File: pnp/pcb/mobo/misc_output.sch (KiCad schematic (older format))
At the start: 45 parts, among them J10 MF3, J11 MF4, J12 DOWNWARDS_LIGHT, J13 UPWARDS_LIGHT, J14 5V_INJECTION, J16 RS-485_2, J17 RS-485_3, J21 AUX1, J22 AUX2, J23 QWIIC1, J24 QWIIC2, J25 RS-485_1, J6 SERVO1, J7 SERVO2, J8 MF1, J9 MF2, Q1 IRF540N, Q2 IRF540N, Q3 IRF540N, Q4 IRF540N, U15 TC4424A, U16 TC4424A, U2 SP3485EN, U3 SP3485EN, U4 SP3485EN

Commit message: Add 24VDC support
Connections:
- net labels added: VDC
- net labels removed: +12V
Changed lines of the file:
@@
 	3325 3050 3325 2850
-$Comp
-L power:+12V #PWR0133
-U 1 1 5EBF89E8
-P 3325 2150
-F 0 "#PWR0133" H 3325 2000 50  0001 C CNN
-F 1 "+12V" H 3340 2323 50  0000 C CNN
-F 2 "" H 3325 2150 50  0001 C CNN
-F 3 "" H 3325 2150 50  0001 C CNN
-	1    3325 2150
-	1    0    0    -1
-$EndComp
 $Comp
 L Device:R_Small R2
@@
 $EndComp
 $Comp
-L power:+12V #PWR0136
-U 1 1 5EC0DF79
-P 3325 3550
-F 0 "#PWR0136" H 3325 3400 50  0001 C CNN
-F 1 "+12V" H 3340 3723 50  0000 C CNN
-F 2 "" H 3325 3550 50  0001 C CNN
-F 3 "" H 3325 3550 50  0001 C CNN
-	1    3325 3550
-	1    0    0    -1
-$EndComp
-$Comp
 L Device:R_Small R3
 U 1 1 5EC0DF80
@@
 $EndComp
 $Comp
-L power:+12V #PWR0139
-U 1 1 5EC1398B
-P 3325 4950
-F 0 "#PWR0139" H 3325 4800 50  0001 C CNN
-F 1 "+12V" H 3340 5123 50  0000 C CNN
-F 2 "" H 3325 4950 50  0001 C CNN
-F 3 "" H 3325 4950 50  0001 C CNN
-	1    3325 4950
-	1    0    0    -1
-$EndComp
-$Comp
 L Device:R_Small R4
 U 1 1 5EC13992
@@
 	1    3125 6550
 	-1   0    0    1
-$EndComp
-$Comp
-L power:+12V #PWR0142
-U 1 1 5EC17A7D
-P 3325 6350
-F 0 "#PWR0142" H 3325 6200 50  0001 C CNN
-F 1 "+12V" H 3340 6523 50  0000 C CNN
-F 2 "" H 3325 6350 50  0001 C CNN
-F 3 "" H 3325 6350 50  0001 C CNN
-	1    3325 6350
-	1    0    0    -1
 $EndComp
 $Comp
@@
 Wire Wire Line
 	3475 2150 3325 2150
-Connection ~ 3325 2150
 Wire Wire Line
 	3325 2250 3325 2150
@@
 Wire Wire Line
 	3475 3550 3325 3550
-Connection ~ 3325 3550
 Wire Wire Line
 	3475 3850 3325 3850
@@
 Wire Wire Line
 	3475 4950 3325 4950
-Connection ~ 3325 4950
 Wire Wire Line
 	3475 5250 3325 5250
@@
 Wire Wire Line
 	3475 6350 3325 6350
-Connection ~ 3325 6350
 $Comp
 L index:TC4424A U15
@@
 $EndComp
 $Comp
-L power:+12V #PWR01
-U 1 1 600410AF
-P 1700 3075
-F 0 "#PWR01" H 1700 2925 50  0001 C CNN
-F 1 "+12V" H 1715 3248 50  0000 C CNN
-F 2 "" H 1700 3075 50  0001 C CNN
-F 3 "" H 1700 3075 50  0001 C CNN
-	1    1700 3075
-	1    0    0    -1
-$EndComp
-$Comp
 L index:TC4424A U16
 U 1 1 6005F5C2
@@
 	1    0    0    -1
 $EndComp
-$Comp
-L power:+12V #PWR03
-U 1 1 6005F5D0
+Wire Wire Line
+	2225 5450 2225 6050
+Wire Wire Line
+	2225 6150 2225 6850
+Wire Wire Line
+	2875 4450 3325 4450
+Connection ~ 3325 4450
+Wire Wire Line
+	2875 3050 3325 3050
+Connection ~ 3325 3050
+Wire Wire Line
+	2875 5850 3325 5850
+Connection ~ 3325 5850
+Wire Wire Line
+	2875 7250 3325 7250
+Connection ~ 3325 7250
+$Comp
+L power:VDC #PWR011
+U 1 1 5FE2C7FC
+P 3325 2150
+F 0 "#PWR011" H 3325 2050 50  0001 C CNN
+F 1 "VDC" H 3340 2323 50  0000 C CNN
+F 2 "" H 3325 2150 50  0001 C CNN
+F 3 "" H 3325 2150 50  0001 C CNN
+	1    3325 2150
+	1    0    0    -1
+$EndComp
+Connection ~ 3325 2150
+$Comp
+L power:VDC #PWR012
+U 1 1 5FE2D669
+P 3325 3550
+F 0 "#PWR012" H 3325 3450 50  0001 C CNN
+F 1 "VDC" H 3340 3723 50  0000 C CNN
+F 2 "" H 3325 3550 50  0001 C CNN
+F 3 "" H 3325 3550 50  0001 C CNN
+	1    3325 3550
+	1    0    0    -1
+$EndComp
+Connection ~ 3325 3550
+$Comp
+L power:VDC #PWR013
+U 1 1 5FE329DB
+P 3325 4950
+F 0 "#PWR013" H 3325 4850 50  0001 C CNN
+F 1 "VDC" H 3340 5123 50  0000 C CNN
+F 2 "" H 3325 4950 50  0001 C CNN
+F 3 "" H 3325 4950 50  0001 C CNN
+	1    3325 4950
+	1    0    0    -1
+$EndComp
+Connection ~ 3325 4950
+$Comp
+L power:VDC #PWR014
+U 1 1 5FE341D0
+P 3325 6350
+F 0 "#PWR014" H 3325 6250 50  0001 C CNN
+F 1 "VDC" H 3340 6523 50  0000 C CNN
+F 2 "" H 3325 6350 50  0001 C CNN
+F 3 "" H 3325 6350 50  0001 C CNN
+	1    3325 6350
+	1    0    0    -1
+$EndComp
+Connection ~ 3325 6350
+$Comp
+L power:+5V #PWR010
+U 1 1 5FE3A03F
 P 1700 5850
-F 0 "#PWR03" H 1700 5700 50  0001 C CNN
-F 1 "+12V" H 1715 6023 50  0000 C CNN
+F 0 "#PWR010" H 1700 5700 50  0001 C CNN
+F 1 "+5V" H 1715 6023 50  0000 C CNN
 F 2 "" H 1700 5850 50  0001 C CNN
 F 3 "" H 1700 5850 50  0001 C CNN
@@
 	1    0    0    -1
 $EndComp
-Wire Wire Line
-	2225 5450 2225 6050
-Wire Wire Line
-	2225 6150 2225 6850
-Wire Wire Line
-	2875 4450 3325 4450
-Connection ~ 3325 4450
-Wire Wire Line
-	2875 3050 3325 3050
-Connection ~ 3325 3050
-Wire Wire Line
-	2875 5850 3325 5850
-Connection ~ 3325 5850
-Wire Wire Line
-	2875 7250 3325 7250
-Connection ~ 3325 7250
+$Comp
+L power:+5V #PWR09
+U 1 1 5FE3AFC7
+P 1700 3075
+F 0 "#PWR09" H 1700 2925 50  0001 C CNN
+F 1 "+5V" H 1715 3248 50  0000 C CNN
+F 2 "" H 1700 3075 50  0001 C CNN
+F 3 "" H 1700 3075 50  0001 C CNN
+	1    1700 3075
+	1    0    0    -1
+$EndComp
 $EndSCHEMATC

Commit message: Replaced freewheeling diodes for more popular diode
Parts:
- removed D6, D7, D8, D9: SM4001, Diode_SMD:D_SOD-123F, symbol Diode:SM4001
- added D6, D7, D8, D9: SM4007, Diode_SMD:D_SOD-123F, symbol Diode:SM4007
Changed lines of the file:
@@
 Wire Wire Line
 	6125 4350 6225 4350
-$Comp
-L Diode:SM4001 D6
-U 1 1 5FE769F9
-P 3475 2300
-F 0 "D6" V 3429 2380 50  0000 L CNN
-F 1 "SM4001" V 3520 2380 50  0000 L CNN
-F 2 "Diode_SMD:D_SOD-123F" H 3475 2125 50  0001 C CNN
-F 3 "http://cdn-reichelt.de/documents/datenblatt/A400/SMD1N400%23DIO.pdf" H 3475 2300 50  0001 C CNN
-	1    3475 2300
-	0    1    1    0
-$EndComp
 Wire Wire Line
 	3475 2150 3325 2150
@@
 	-1   0    0    1
 $EndComp
-$Comp
-L Diode:SM4001 D7
-U 1 1 5FEE58D0
-P 3475 3700
-F 0 "D7" V 3429 3780 50  0000 L CNN
-F 1 "SM4001" V 3520 3780 50  0000 L CNN
-F 2 "Diode_SMD:D_SOD-123F" H 3475 3525 50  0001 C CNN
-F 3 "http://cdn-reichelt.de/documents/datenblatt/A400/SMD1N400%23DIO.pdf" H 3475 3700 50  0001 C CNN
-	1    3475 3700
-	0    1    1    0
-$EndComp
 Wire Wire Line
 	3475 3550 3325 3550
@@
 	3475 3850 3325 3850
 Connection ~ 3325 3850
-$Comp
-L Diode:SM4001 D8
-U 1 1 5FF2A1C6
-P 3475 5100
-F 0 "D8" V 3429 5180 50  0000 L CNN
-F 1 "SM4001" V 3520 5180 50  0000 L CNN
-F 2 "Diode_SMD:D_SOD-123F" H 3475 4925 50  0001 C CNN
-F 3 "http://cdn-reichelt.de/documents/datenblatt/A400/SMD1N400%23DIO.pdf" H 3475 5100 50  0001 C CNN
-	1    3475 5100
-	0    1    1    0
-$EndComp
 Wire Wire Line
 	3325 5050 3325 4950
@@
 	3475 5250 3325 5250
 Connection ~ 3325 5250
-$Comp
-L Diode:SM4001 D9
-U 1 1 5FF3FCAF
-P 3475 6500
-F 0 "D9" V 3429 6580 50  0000 L CNN
-F 1 "SM4001" V 3520 6580 50  0000 L CNN
-F 2 "Diode_SMD:D_SOD-123F" H 3475 6325 50  0001 C CNN
-F 3 "http://cdn-reichelt.de/documents/datenblatt/A400/SMD1N400%23DIO.pdf" H 3475 6500 50  0001 C CNN
-	1    3475 6500
-	0    1    1    0
-$EndComp
 Wire Wire Line
 	3475 6650 3325 6650
@@
 	1    0    0    -1
 $EndComp
+$Comp
+L Diode:SM4007 D6
+U 1 1 5FE627BC
+P 3475 2300
+F 0 "D6" V 3429 2380 50  0000 L CNN
+F 1 "SM4007" V 3520 2380 50  0000 L CNN
+F 2 "Diode_SMD:D_SOD-123F" H 3475 2125 50  0001 C CNN
+F 3 "http://cdn-reichelt.de/documents/datenblatt/A400/SMD1N400%23DIO.pdf" H 3475 2300 50  0001 C CNN
+	1    3475 2300
+	0    1    1    0
+$EndComp
+$Comp
+L Diode:SM4007 D7
+U 1 1 5FE700E2
+P 3475 3700
+F 0 "D7" V 3429 3780 50  0000 L CNN
+F 1 "SM4007" V 3520 3780 50  0000 L CNN
+F 2 "Diode_SMD:D_SOD-123F" H 3475 3525 50  0001 C CNN
+F 3 "http://cdn-reichelt.de/documents/datenblatt/A400/SMD1N400%23DIO.pdf" H 3475 3700 50  0001 C CNN
+	1    3475 3700
+	0    1    1    0
+$EndComp
+$Comp
+L Diode:SM4007 D8
+U 1 1 5FE71865
+P 3475 5100
+F 0 "D8" V 3429 5180 50  0000 L CNN
+F 1 "SM4007" V 3520 5180 50  0000 L CNN
+F 2 "Diode_SMD:D_SOD-123F" H 3475 4925 50  0001 C CNN
+F 3 "http://cdn-reichelt.de/documents/datenblatt/A400/SMD1N400%23DIO.pdf" H 3475 5100 50  0001 C CNN
+	1    3475 5100
+	0    1    1    0
+$EndComp
+$Comp
+L Diode:SM4007 D9
+U 1 1 5FE75BA6
+P 3475 6500
+F 0 "D9" V 3429 6580 50  0000 L CNN
+F 1 "SM4007" V 3520 6580 50  0000 L CNN
+F 2 "Diode_SMD:D_SOD-123F" H 3475 6325 50  0001 C CNN
+F 3 "http://cdn-reichelt.de/documents/datenblatt/A400/SMD1N400%23DIO.pdf" H 3475 6500 50  0001 C CNN
+	1    3475 6500
+	0    1    1    0
+$EndComp
 $EndSCHEMATC

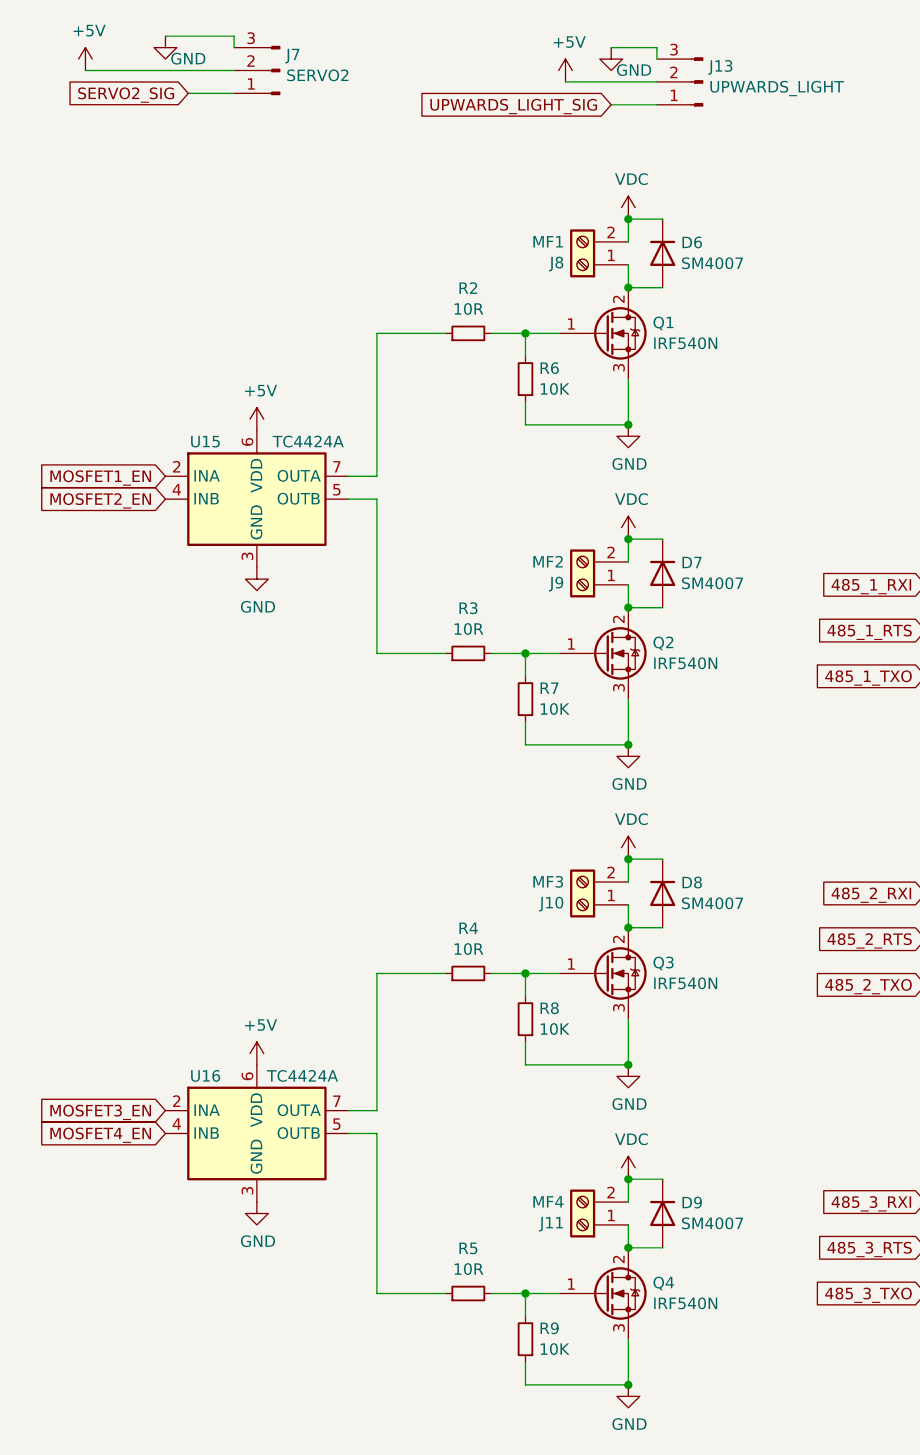
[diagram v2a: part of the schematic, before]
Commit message: Replace MOSFETs and organized vacuum sensor
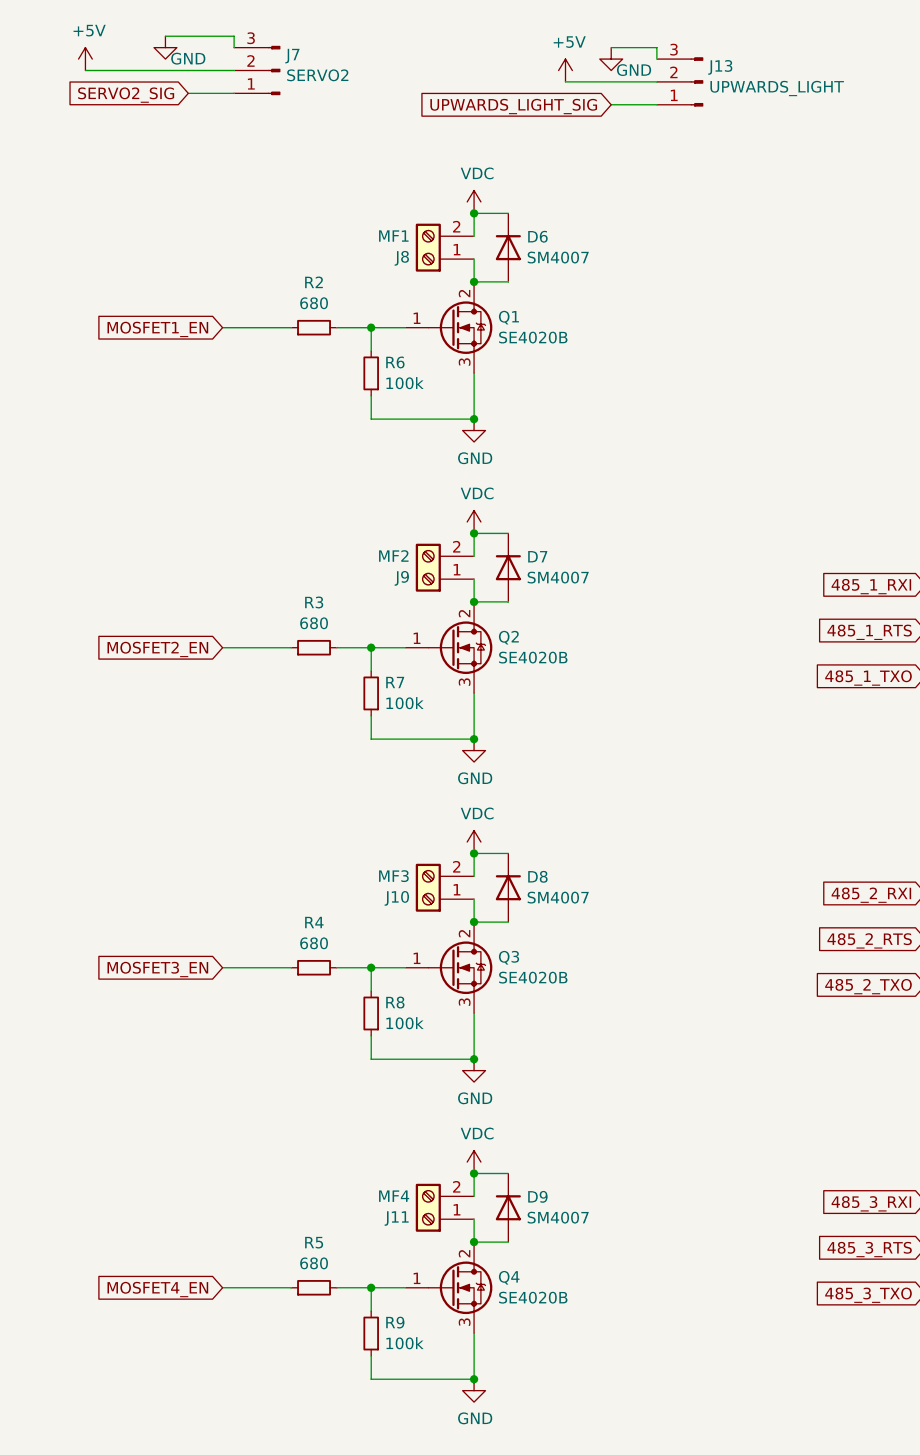
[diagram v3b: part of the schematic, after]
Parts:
- removed Q1, Q2, Q3, Q4: IRF540N, Package_TO_SOT_SMD:TO-252-2, symbol Transistor_FET:IRF540N
- removed U15, U16: TC4424A, Package_SO:SOIC-8_3.9x4.9mm_P1.27mm, symbol index:TC4424A
- added Q1, Q2, Q3, Q4: SE4020B, Package_TO_SOT_SMD:TO-252-2, symbol index:SE4020B
- R10, R11, R12, R37: footprint Resistor_SMD:R_0805_2012Metric_Pad1.15x1.40mm_HandSolder -> Resistor_SMD:R_0805_2012Metric_Pad1.20x1.40mm_HandSolder
- R2, R3, R4, R5: value 10R -> 680; footprint Resistor_SMD:R_0805_2012Metric_Pad1.15x1.40mm_HandSolder -> Resistor_SMD:R_0805_2012Metric_Pad1.20x1.40mm_HandSolder
- R6, R7, R8, R9: value 10K -> 100k; footprint Resistor_SMD:R_0805_2012Metric_Pad1.15x1.40mm_HandSolder -> Resistor_SMD:R_0805_2012Metric_Pad1.20x1.40mm_HandSolder
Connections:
- net GND: now also Q1.3 (S), Q2.3 (S), Q3.3 (S), Q4.3 (S)
- net MOSFET1_EN: now also R2.1
- net MOSFET2_EN: now also R3.1
- net MOSFET3_EN: now also R4.1
- net MOSFET4_EN: now also R5.1
- net at R2.2, R6.2: now also Q1.1 (G)
- net at D6.2 (A), J8.1 (Pin_1): now also Q1.2 (D)
- net at R3.2, R7.2: now also Q2.1 (G)
- net at D7.2 (A), J9.1 (Pin_1): now also Q2.2 (D)
- net at R4.2, R8.2: now also Q3.1 (G)
- net at D8.2 (A), J10.1 (Pin_1): now also Q3.2 (D)
- net at R5.2, R9.2: now also Q4.1 (G)
- net at D9.2 (A), J11.1 (Pin_1): now also Q4.2 (D)
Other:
- moved on the sheet: D6, D7, D8, D9, J10, J11, J8, J9, R2, R3, R4, R5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

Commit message: Revert "Replace MOSFETs and organized vacuum sensor"
This reverts commit d845c98ea56ba571b636da2743323a7f663cddfe.
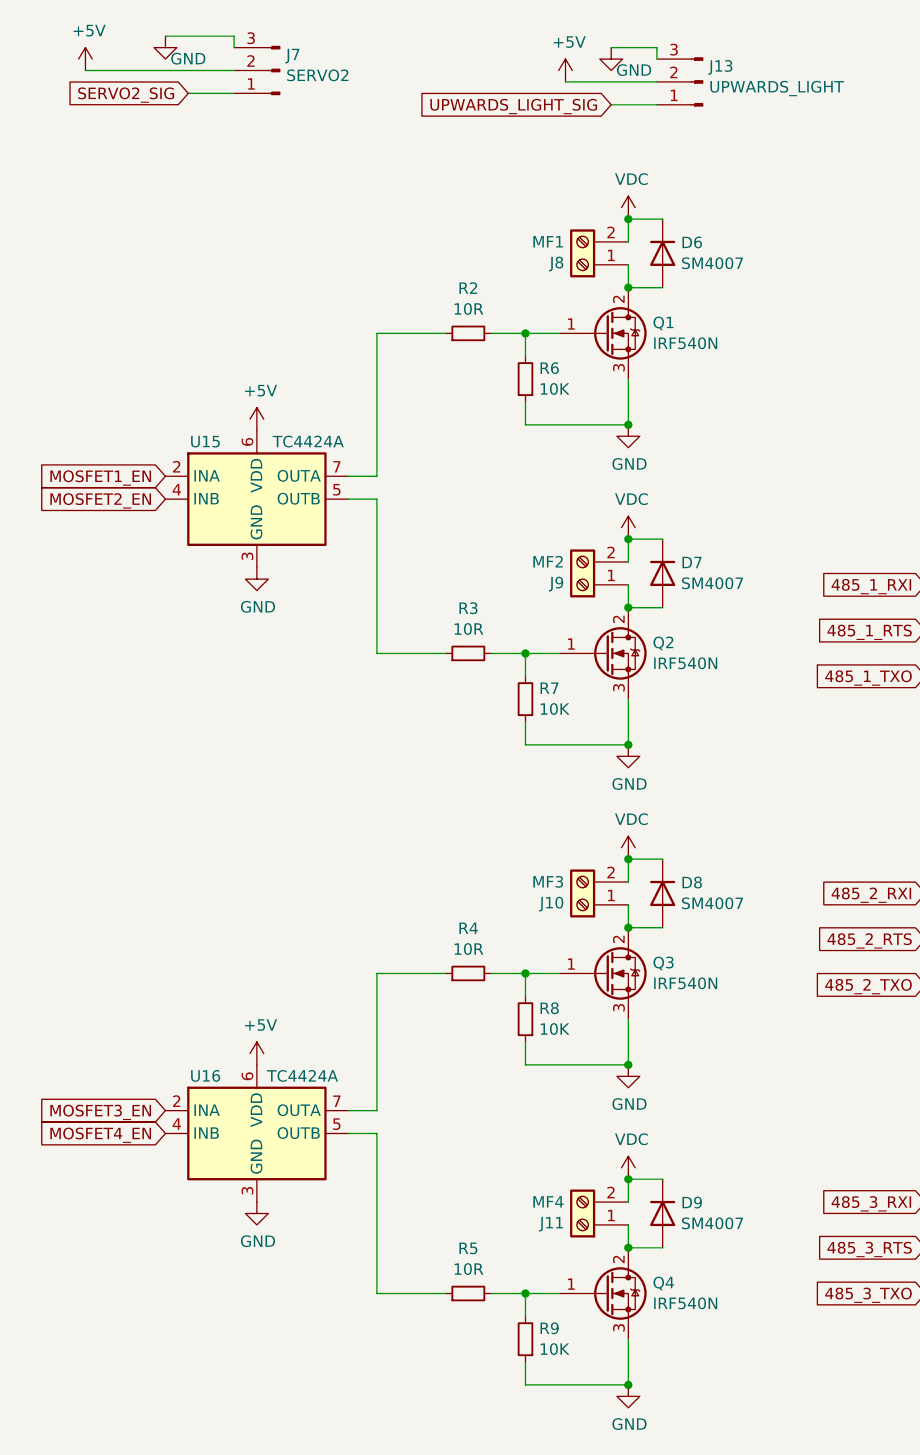
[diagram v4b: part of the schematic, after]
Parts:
- removed Q1, Q2, Q3, Q4: SE4020B, Package_TO_SOT_SMD:TO-252-2, symbol index:SE4020B
- added Q1, Q2, Q3, Q4: IRF540N, Package_TO_SOT_SMD:TO-252-2, symbol Transistor_FET:IRF540N
- added U15, U16: TC4424A, Package_SO:SOIC-8_3.9x4.9mm_P1.27mm, symbol index:TC4424A
- R10, R11, R12, R37: footprint Resistor_SMD:R_0805_2012Metric_Pad1.20x1.40mm_HandSolder -> Resistor_SMD:R_0805_2012Metric_Pad1.15x1.40mm_HandSolder
- R2, R3, R4, R5: value 680 -> 10R; footprint Resistor_SMD:R_0805_2012Metric_Pad1.20x1.40mm_HandSolder -> Resistor_SMD:R_0805_2012Metric_Pad1.15x1.40mm_HandSolder
- R6, R7, R8, R9: value 100k -> 10K; footprint Resistor_SMD:R_0805_2012Metric_Pad1.20x1.40mm_HandSolder -> Resistor_SMD:R_0805_2012Metric_Pad1.15x1.40mm_HandSolder
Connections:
- net +5V: now also U15.6 (VDD), U16.6 (VDD)
- net GND: now also Q1.3 (S), Q2.3 (S), Q3.3 (S), Q4.3 (S), U15.3 (GND), U16.3 (GND)
- net MOSFET1_EN: now also U15.2 (INA); no longer R2.1
- net MOSFET2_EN: now also U15.4 (INB); no longer R3.1
- net MOSFET3_EN: now also U16.2 (INA); no longer R4.1
- net MOSFET4_EN: now also U16.4 (INB); no longer R5.1
- net at R2.2, R6.2: now also Q1.1 (G)
- net at D6.2 (A), J8.1 (Pin_1): now also Q1.2 (D)
- net at R3.2, R7.2: now also Q2.1 (G)
- net at D7.2 (A), J9.1 (Pin_1): now also Q2.2 (D)
- net at R4.2, R8.2: now also Q3.1 (G)
- net at D8.2 (A), J10.1 (Pin_1): now also Q3.2 (D)
- net at R5.2, R9.2: now also Q4.1 (G)
- net at D9.2 (A), J11.1 (Pin_1): now also Q4.2 (D)
- new net: R2.1, U15.7 (OUTA)
- new net: R3.1, U15.5 (OUTB)
- new net: R4.1, U16.7 (OUTA)
- new net: R5.1, U16.5 (OUTB)
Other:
- moved on the sheet: D6, D7, D8, D9, J10, J11, J8, J9, R2, R3, R4, R5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
